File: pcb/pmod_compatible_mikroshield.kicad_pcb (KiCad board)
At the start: 2 copper layers, 25.4 x 28.6 mm, 10 parts, among them J1 CON_HDR_MIKROBUS_ADDON_TH, J2 CON_HDR_100MILS_F_TH_RA_2X6, J3 CON_HDR_100MILS_M_TH_1X3, J4 CON_HDR_100MILS_M_TH_1X2, J5 CON_HDR_100MILS_M_TH_1X2

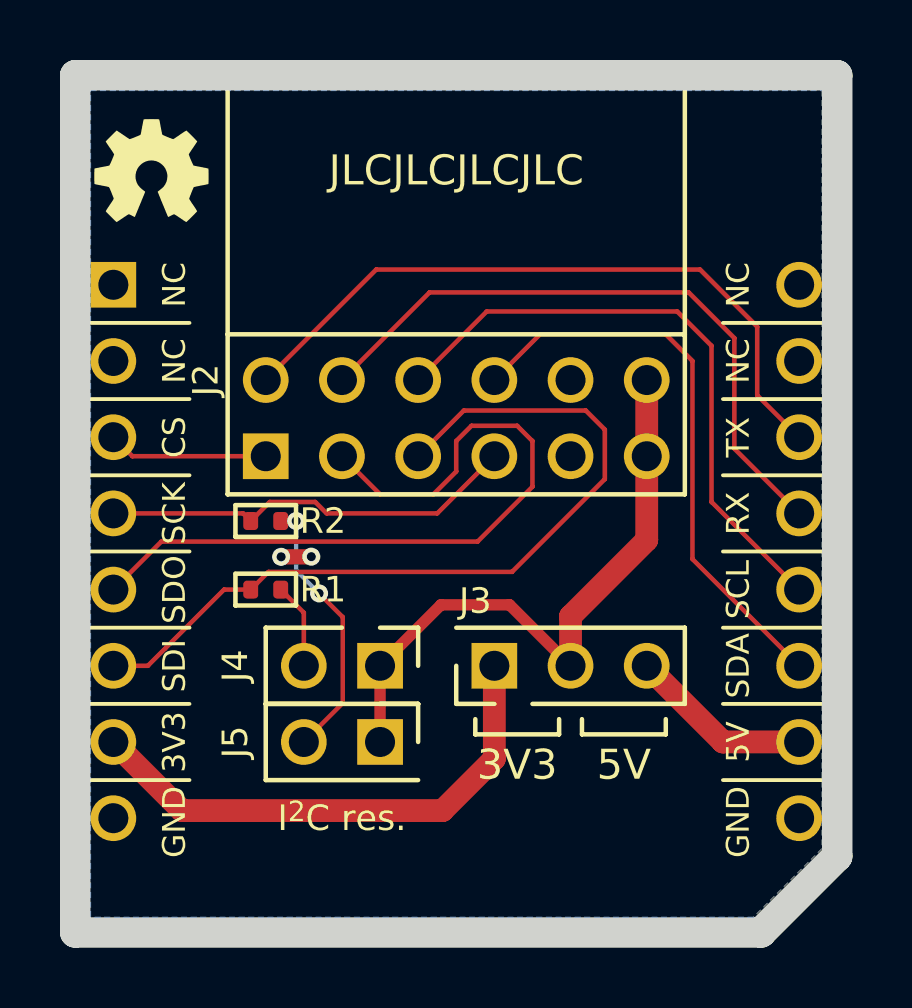
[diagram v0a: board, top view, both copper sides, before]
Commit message: Fix name compliance with Pmod license Add RoHS logo Fix pin names
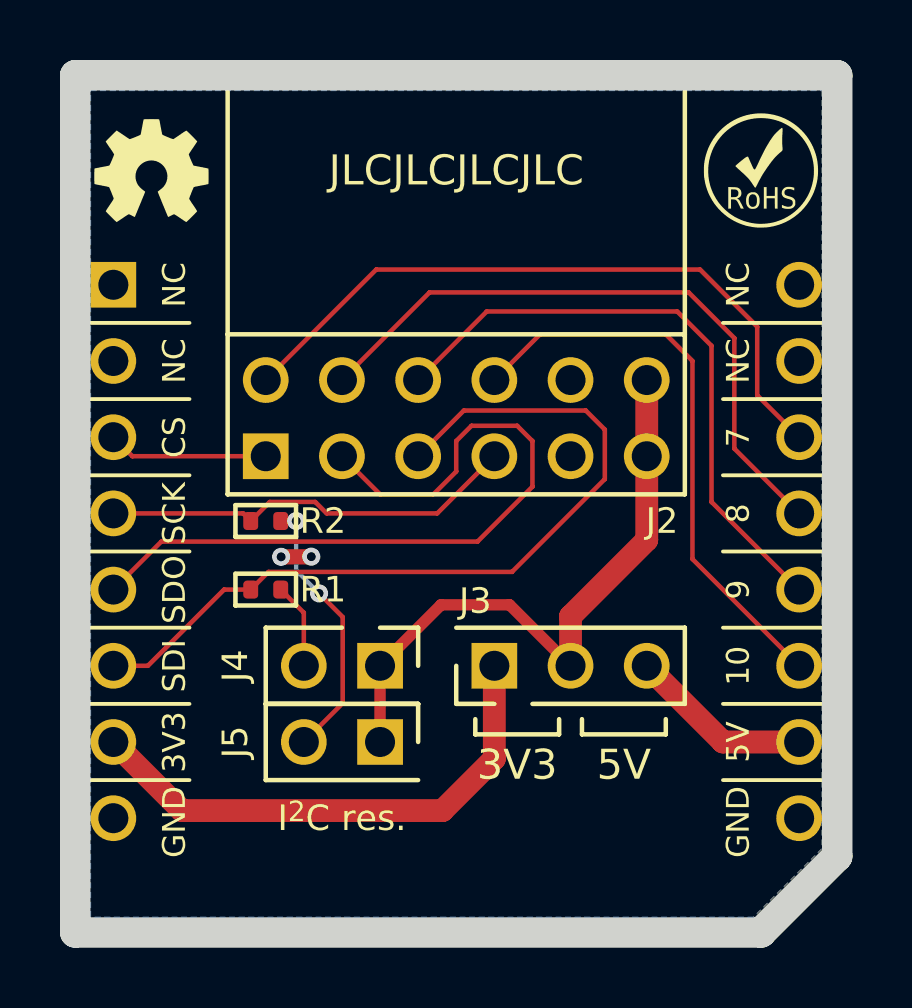
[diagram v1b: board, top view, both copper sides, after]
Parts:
- added G***: LOGO, LOGO, F.Cu at (149.9, 101.6)
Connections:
- J1 pad 11: /IO9 -> /IO7
- J1 pad 12: /IO10 -> /IO8
- J1 pad 13: /IO18 -> /IO9
- J1 pad 14: /IO23 -> /IO10
- J2 pad 10: /IO23 -> /IO10
- J2 pad 7: /IO9 -> /IO7
- J2 pad 8: /IO10 -> /IO8
- J2 pad 9: /IO18 -> /IO9
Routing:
- net /IO7: track 0.00 -> 23.0 mm
- net /IO8: track 0.00 -> 21.7 mm
- net /IO18: track 20.5 -> 0.00 mm
- net /IO23: track 19.2 -> 0.00 mm
- net /IO9: track 23.0 -> 20.5 mm
- net /IO10: track 21.7 -> 19.2 mm
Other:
- board text added: "Digilent Pmod^{TM} Compatible Rev ${rev} ${year}-${month} Licensed under CERN-OHL-W v2"
- board text removed: "${title} Rev ${rev} ${year}-${month} Licensed under CERN-OHL-W v2"

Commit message: Fix inverted SDO/SDI Add source resistors to signal lines
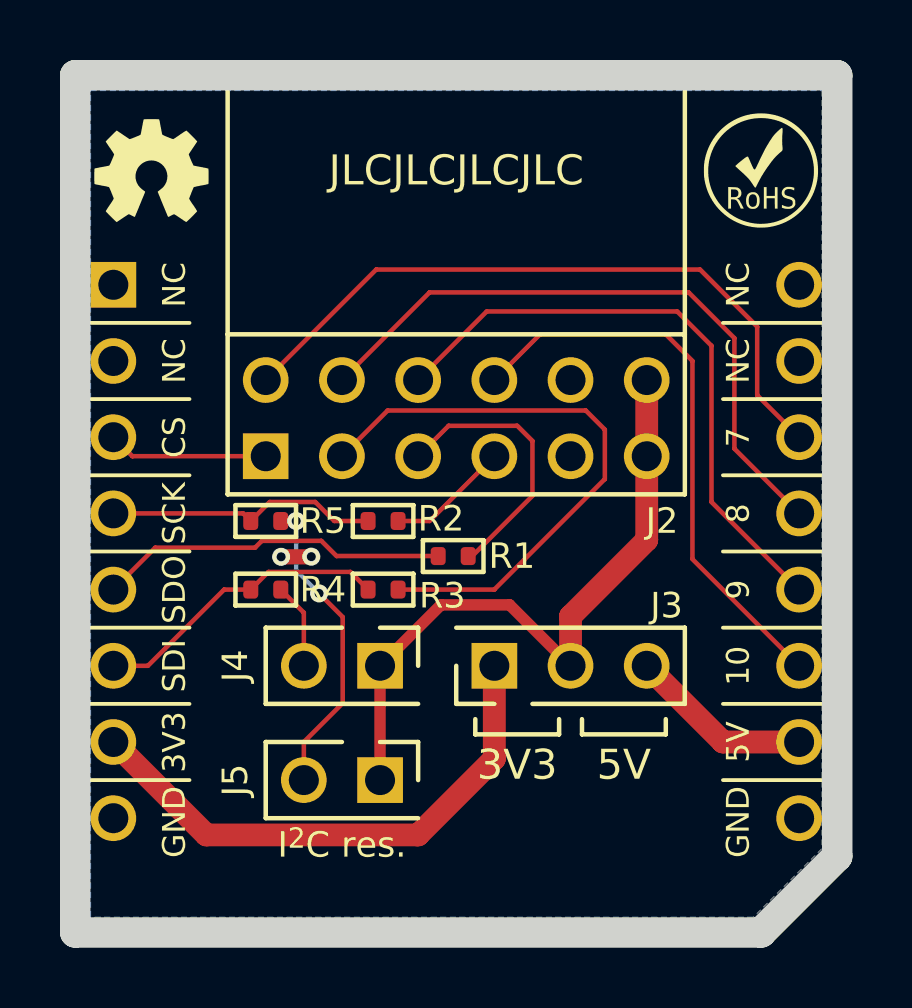
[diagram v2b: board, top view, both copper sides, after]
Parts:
- added R1: RES_49.9Ω_1%_0402, connaxio-resistors:RES_0402_1005M, F.Cu at (139.6, 114.5)
- added R2: RES_49.9Ω_1%_0402, connaxio-resistors:RES_0402_1005M, F.Cu at (137.3, 113.3)
- added R3: RES_49.9Ω_1%_0402, connaxio-resistors:RES_0402_1005M, F.Cu at (137.3, 115.6)
- R4: renamed from R1; value RES_1.00KΩ_1%_0402 -> RES_1.54KΩ_1%_0402
- R5: renamed from R2; value RES_1.00KΩ_1%_0402 -> RES_1.54KΩ_1%_0402
- moved J5 1.27 mm to (135.9, 121.9)
- moved G*** 0.25 mm to (139.7, 124.7)
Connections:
- J2 pad 2: /SDO -> Net-(J2-Pad2)
- J2 pad 3: /SDI -> Net-(J2-Pad3)
- J2 pad 4: /SCK -> Net-(J2-Pad4)
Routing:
- net Net-(J2-Pad2): track 0.00 -> 19.7 mm
- net /SDI: track 27.7 -> 10.0 mm
- net /SDO: track 25.5 -> 11.7 mm
- net Net-(J2-Pad3): track 0.00 -> 9.24 mm
- net /SCK: track 14.0 -> 9.12 mm
- net Net-(J2-Pad4): track 0.00 -> 4.10 mm
- net Net-(J5-Pad2): track 9.06 -> 10.3 mm
- net /VCC: track 21.2 -> 22.4 mm
- net +3.3VA: track 17.5 -> 18.1 mm
